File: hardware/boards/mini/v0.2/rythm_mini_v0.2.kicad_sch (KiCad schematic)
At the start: 84 parts, among them IC1 NAU88C22YG, IC3 IS42S16160J-6BLI, Q1 PMV37EN22, U1 W25Q128JVP, U2 LTV-217-G, U3 RythmMini, U4 STM32H750XBHx, U5 MT48LC32M8A2TG, Y1 Crystal_GND24

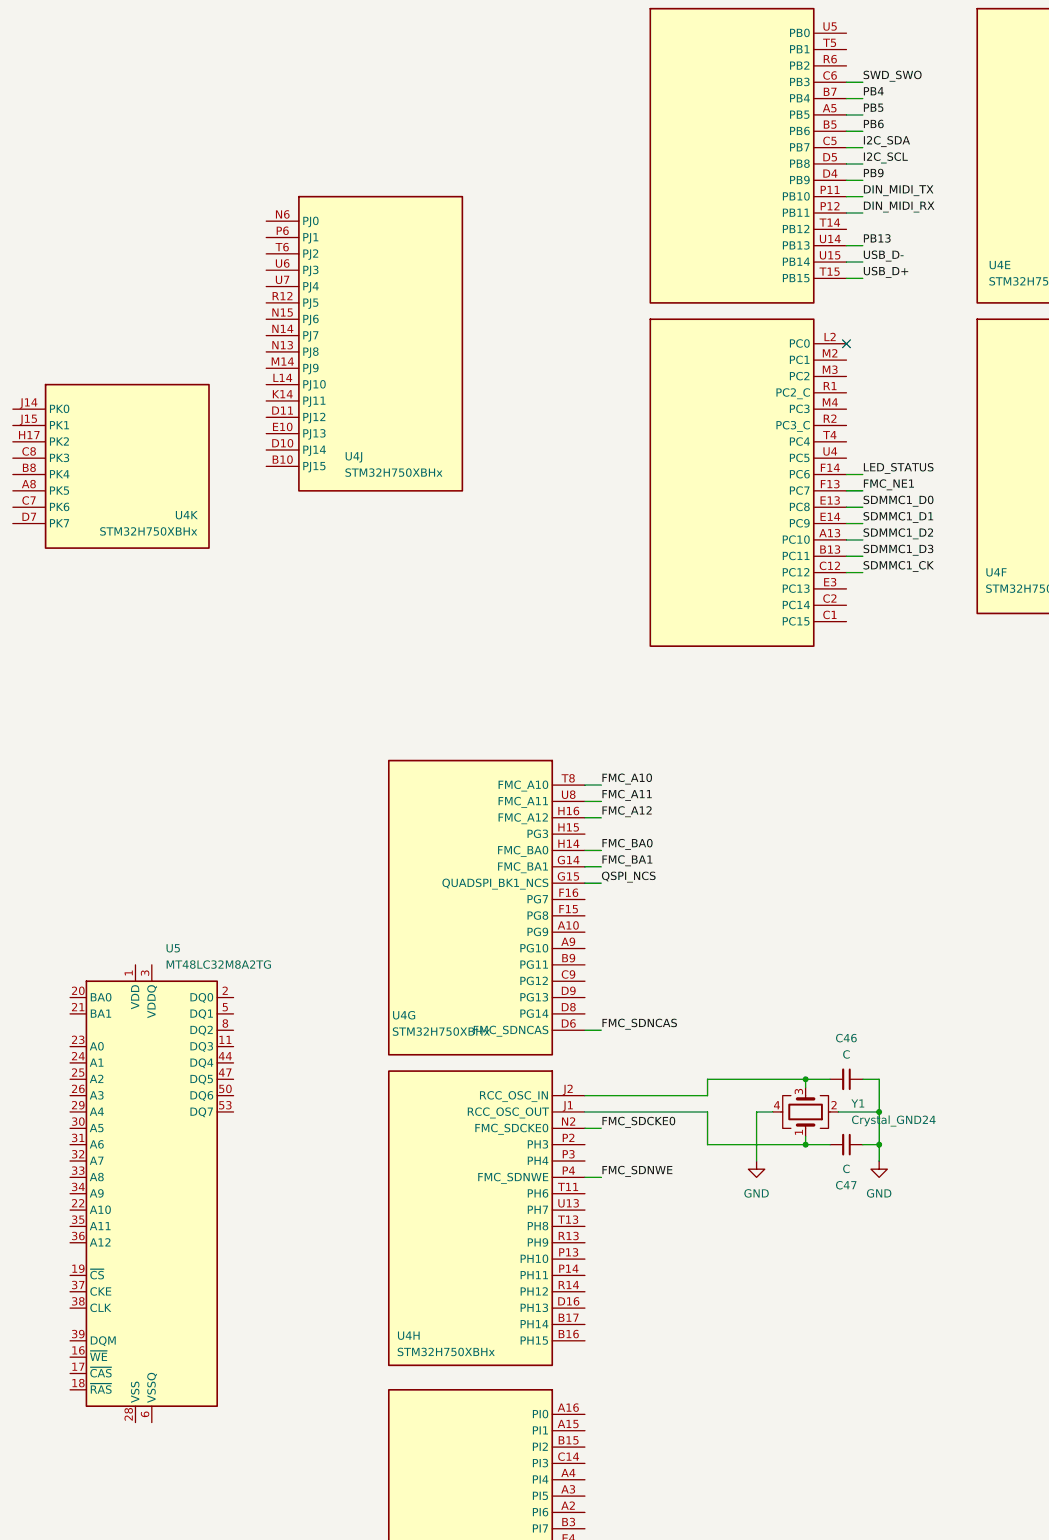
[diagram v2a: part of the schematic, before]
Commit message: mini: route codec, SDMMC, and MIDI in/out
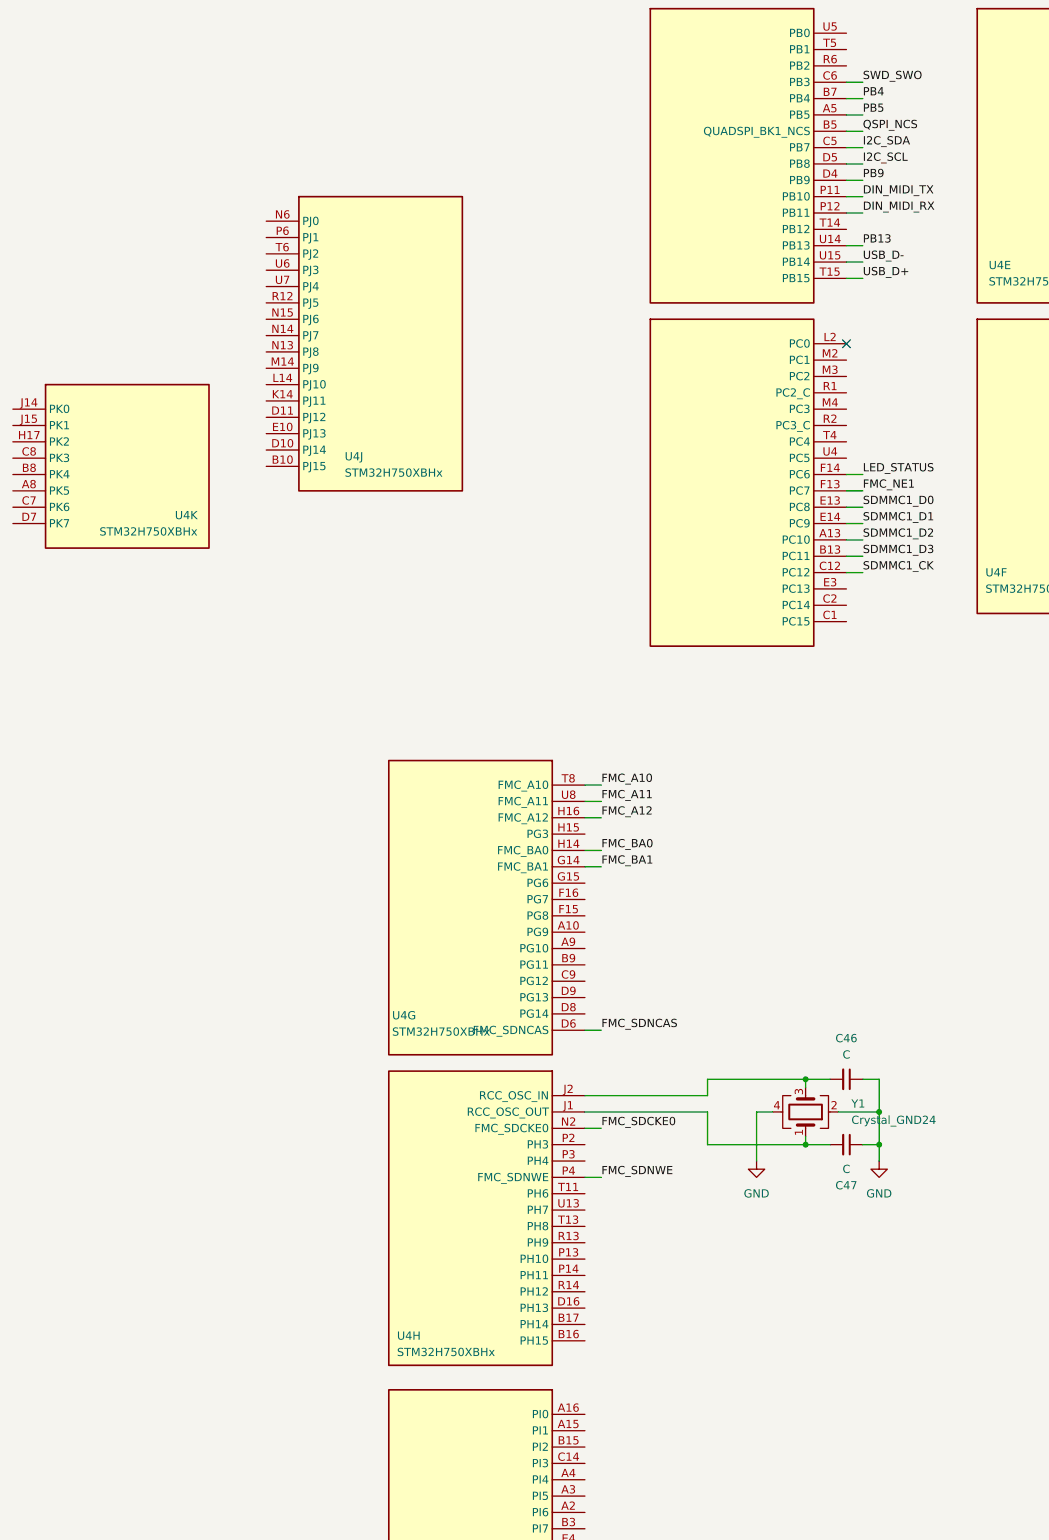
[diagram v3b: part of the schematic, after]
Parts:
- removed U5: MT48LC32M8A2TG, Package_SO:TSOP-II-54_22.2x10.16mm_P0.8mm, symbol Memory_RAM:MT48LC32M8A2TG
- C46, C47: footprint (none) -> Capacitor_SMD:C_0402_1005Metric
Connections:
- net PB6: no longer U4.B5 (PB6)
- net QSPI_NCS: now also U4.B5 (PB6); no longer U4.G15 (PG6)
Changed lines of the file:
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@@
 	(wire
 		(pts
-			(xy 50.8 110.49) (xy 53.34 110.49)
-		)
-		(stroke
-			(width 0)
-			(type default)
-		)
-	)
-	(wire
-		(pts
 			(xy 271.78 85.09) (xy 271.78 87.63)
 		)
@@
 	(wire
 		(pts
-			(xy 10.16 227.33) (xy 12.7 227.33)
+			(xy 50.8 110.49) (xy 53.34 110.49)
 		)
 		(stroke
@@
 	)
 	(label "QSPI_NCS"
-		(at 12.7 227.33 0)
+		(at 53.34 110.49 0)
 		(effects
 			(font
@@
 		)
 	)
-	(label "PB6"
-		(at 53.34 110.49 0)
-		(effects
-			(font
-				(size 1.27 1.27)
-			)
-			(justify left bottom)
-		)
-	)
 	(label "LED_STATUS2"
 		(at 375.92 273.05 180)
@@
 	)
 	(symbol
-		(lib_id "Memory_RAM:MT48LC32M8A2TG")
-		(at -57.15 275.59 0)
-		(unit 1)
-		(exclude_from_sim no)
-		(in_bom yes)
-		(on_board yes)
-		(dnp no)
-		(fields_autoplaced yes)
-		(property "Reference" "U5"
-			(at -55.0067 237.49 0)
-			(effects
-				(font
-					(size 1.27 1.27)
-				)
-				(justify left)
-			)
-		)
-		(property "Value" "MT48LC32M8A2TG"
-			(at -55.0067 240.03 0)
-			(effects
-				(font
-					(size 1.27 1.27)
-				)
-				(justify left)
-			)
-		)
-		(property "Footprint" "Package_SO:TSOP-II-54_22.2x10.16mm_P0.8mm"
-			(at -57.15 311.15 0)
-			(effects
-				(font
-					(size 1.27 1.27)
-					(italic yes)
-				)
-				(hide yes)
-			)
-		)
-		(property "Datasheet" "https://www.micron.com/-/media/client/global/documents/products/data-sheet/dram/256mb_sdr.pdf"
-			(at -57.15 281.94 0)
-			(effects
-				(font
-					(size 1.27 1.27)
-				)
-				(hide yes)
-			)
-		)
-		(property "Description" "256M – (32M x 8 bit) Synchronous DRAM (SDRAM), TSOP-II-54"
-			(at -57.15 275.59 0)
-			(effects
-				(font
-					(size 1.27 1.27)
-				)
-				(hide yes)
-			)
-		)
-		(pin "30"
-		)
-		(pin "18"
-		)
-		(pin "23"
-		)
-		(pin "24"
-		)
-		(pin "12"
-		)
-		(pin "22"
-		)
-		(pin "34"
-		)
-		(pin "47"
-		)
-		(pin "16"
-		)
-		(pin "28"
-		)
-		(pin "17"
-		)
-		(pin "50"
-		)
-		(pin "26"
-		)
-		(pin "44"
-		)
-		(pin "13"
-		)
-		(pin "29"
-		)
-		(pin "37"
-		)
-		(pin "41"
-		)
-		(pin "46"
-		)
-		(pin "32"
-		)
-		(pin "45"
-		)
-		(pin "52"
-		)
-		(pin "14"
-		)
-		(pin "49"
-		)
-		(pin "7"
-		)
-		(pin "27"
-		)
-		(pin "9"
-		)
-		(pin "48"
-		)
-		(pin "25"
-		)
-		(pin "10"
-		)
-		(pin "6"
-		)
-		(pin "8"
-		)
-		(pin "33"
-		)
-		(pin "5"
-		)
-		(pin "42"
-		)
-		(pin "2"
-		)
-		(pin "40"
-		)
-		(pin "4"
-		)
-		(pin "51"
-		)
-		(pin "1"
-		)
-		(pin "35"
-		)
-		(pin "53"
-		)
-		(pin "43"
-		)
-		(pin "21"
-		)
-		(pin "3"
-		)
-		(pin "54"
-		)
-		(pin "36"
-		)
-		(pin "19"
-		)
-		(pin "31"
-		)
-		(pin "39"
-		)
-		(pin "15"
-		)
-		(pin "20"
-		)
-		(pin "38"
-		)
-		(pin "11"
-		)
-		(instances
-			(project ""
-				(path "/f8dd7a9e-fcd3-404d-b8a5-ab89fe05940b"
-					(reference "U5")
-					(unit 1)
-				)
-			)
-		)
-	)
-	(symbol
 		(lib_id "Device:C_Small")
 		(at 388.62 158.75 90)
@@
 		)
 		(pin "G15"
-			(alternate "QUADSPI_BK1_NCS")
 		)
 		(pin "F16"
@@
 		)
 		(pin "B5"
+			(alternate "QUADSPI_BK1_NCS")
 		)
 		(pin "C5"
@@
 			)
 		)
-		(property "Footprint" ""
+		(property "Footprint" "Capacitor_SMD:C_0402_1005Metric"
 			(at 50.8 267.97 0)
 			(effects
@@
 			)
 		)
-		(property "Footprint" ""
+		(property "Footprint" "Capacitor_SMD:C_0402_1005Metric"
 			(at 50.8 257.81 0)
 			(effects
